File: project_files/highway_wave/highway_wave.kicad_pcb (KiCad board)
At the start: 2 copper layers, 138.2 x 87.8 mm, 36 parts, among them J1 Screw_Terminal_01x02, J10 Conn_01x02_Socket, J11 Conn_01x24, J12 Conn_01x24, J13 Screw_Terminal_01x02, J2 Screw_Terminal_01x02, J3 Conn_01x02_Socket, J4 Conn_01x02_Socket, J5 Conn_01x02_Pin, J6 Conn_01x02_Pin, J7 Conn_01x02_Pin, J8 Conn_01x04_Socket, J9 Conn_01x02_Pin, U1 TPS75633KC, U2 MOUDLE-BLUETOOTH-AUDIO-BC127_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, U4 PAM8403D

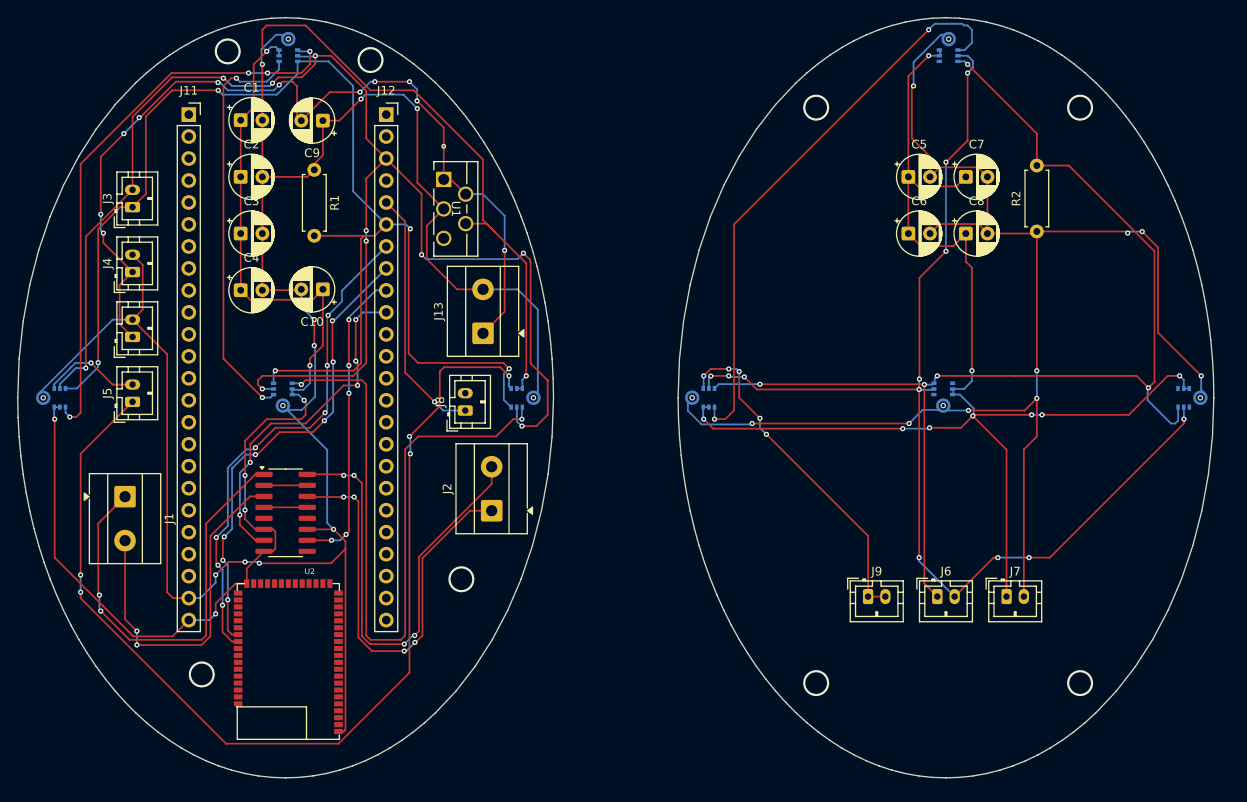
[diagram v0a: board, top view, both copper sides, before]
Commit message: moved caps on PCB
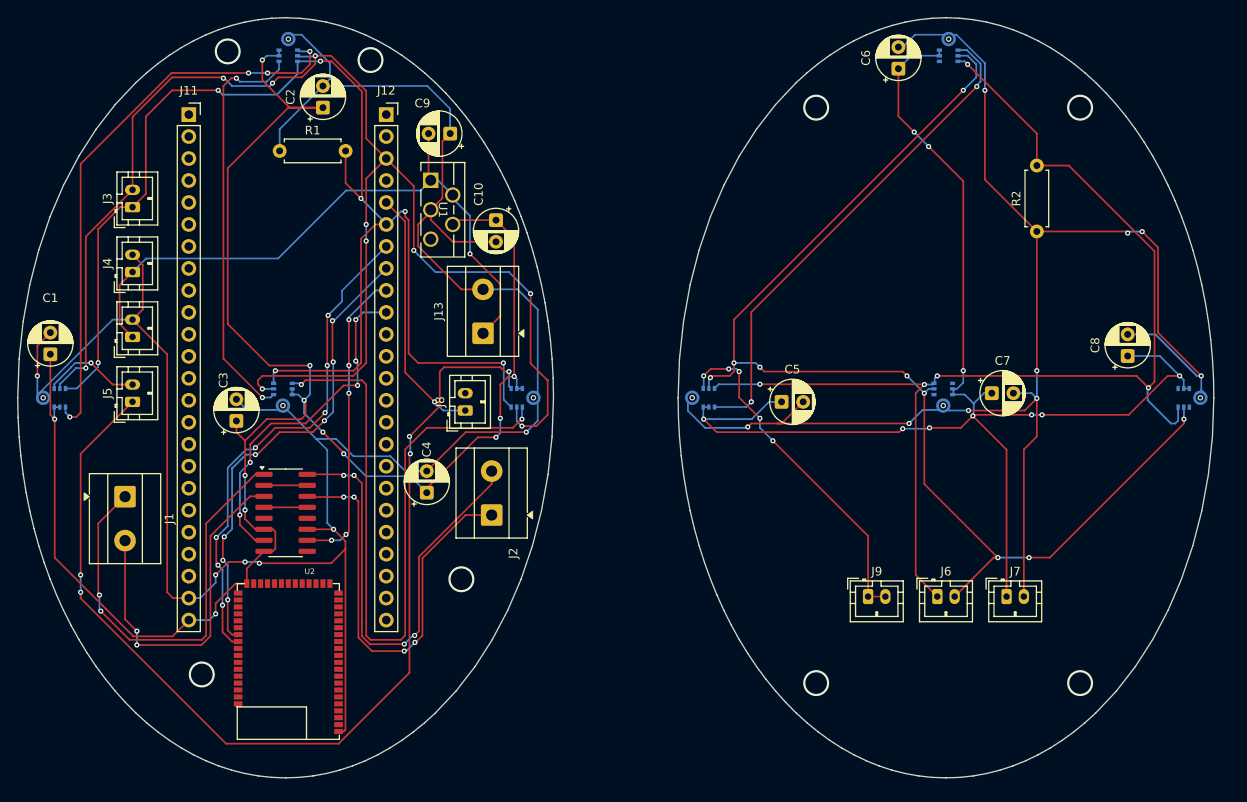
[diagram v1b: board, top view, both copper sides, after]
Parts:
- moved C1 34.9 mm to (74.0, 86.0), turned to 90 degrees
- moved C4 31.8 mm to (117.5, 102.0), turned to 90 degrees
- moved C5 29.8 mm to (158.5, 91.5)
- moved C7 25.2 mm to (182.8, 90.5)
- moved C8 23.5 mm to (198.5, 86.2), turned to 90 degrees
- moved C3 21.7 mm to (95.5, 93.7), turned to 90 degrees
- moved C10 21.5 mm to (125.5, 70.5), turned to -90 degrees
- moved C6 19.1 mm to (172.0, 53.0), turned to 90 degrees
- moved C9 14.8 mm to (120.2, 60.5)
- moved C2 12.4 mm to (105.5, 57.5), turned to 90 degrees
- moved R1 4.56 mm to (100.5, 62.5), turned to 0 degrees
- moved U1 1.50 mm to (118.0, 65.9)
- moved J2 0.50 mm to (125.0, 104.6)
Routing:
- net IN_3V3: track 105.8 -> 75.6 mm, vias 11 -> 1
- net Vout from Bat reg: track 204.5 -> 217.5 mm, vias 8 -> 12
- net IN_GND: track 245.9 -> 257.1 mm, vias 9 -> 6
- net WSO Mk5: track 66.3 -> 57.8 mm
- net Net-(J7-Pin_1): track 148.4 -> 156.5 mm, vias 9 -> 10
- net Net-(J6-Pin_2): track 133.0 -> 137.9 mm, vias 12 -> 9
- net Net-(J7-Pin_2): track 165.7 -> 169.8 mm
- net 36_IOB29B: track 170.7 -> 168.2 mm
- net 26_IOB8B: track 153.9 -> 156.1 mm, vias 5 -> 7
- net Net-(J6-Pin_1): track 134.5 -> 135.3 mm
- net Net-(J2-Pin_2): track 54.5 -> 54.0 mm
- net Net-(J2-Pin_1): track 49.9 -> 50.4 mm
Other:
- board text added: "(L)"
- board text added: "(R)"
- board text added: "w a v e"

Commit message: update BOM
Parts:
- removed C10: 47 uF, Capacitor_THT:CP_Radial_D5.0mm_P2.50mm
- removed C9: 1 uF, Capacitor_THT:CP_Radial_D5.0mm_P2.50mm
- removed the J1 at (82.6, 102.5)
- removed the J10 at (83.5, 84.0)
- removed the J2 at (125.0, 104.6)
- removed the J4 at (83.5, 76.5)
- removed U1: TPS75633KC, footprints:KC5
- removed U2: MOUDLE-BLUETOOTH-AUDIO-BC127_51P-18X11.8MM_, MOUDLE-BLUETOOTH-AUDIO-BC127_51P-18X11.8MM_:LGA51-0.8-18X11.8MM
- removed U4: PAM8403D, Package_SO:SOP-16_3.9x9.9mm_P1.27mm
- added J11: Conn_01x02_Socket, Connector_JST:JST_PH_B2B-PH-K_1x02_P2.00mm_Vertical, F.Cu at (118.0, 84.0)
- added J12: Conn_01x02_Socket, Connector_JST:JST_PH_B2B-PH-K_1x02_P2.00mm_Vertical, F.Cu at (117.9, 90.6)
- added J14: Conn_01x02_Socket, Connector_JST:JST_PH_B2B-PH-K_1x02_P2.00mm_Vertical, F.Cu at (83.0, 111.5)
- added J15: Conn_01x02_Socket, Connector_JST:JST_PH_B2B-PH-K_1x02_P2.00mm_Vertical, F.Cu at (83.0, 118.0)
- added J16: Conn_01x02_Socket, Connector_JST:JST_PH_B2B-PH-K_1x02_P2.00mm_Vertical, F.Cu at (118.0, 97.5)
- added J17: Conn_01x02_Socket, Connector_JST:JST_PH_B2B-PH-K_1x02_P2.00mm_Vertical, F.Cu at (118.0, 104.0)
- added J18: Conn_01x02_Socket, Connector_JST:JST_PH_B2B-PH-K_1x02_P2.00mm_Vertical, F.Cu at (125.5, 95.5)
- added J19: Conn_01x02_Socket, Connector_JST:JST_PH_B2B-PH-K_1x02_P2.00mm_Vertical, F.Cu at (118.0, 62.4)
- added J20: Screw_Terminal_01x02, TerminalBlock_MetzConnect:TerminalBlock_MetzConnect_Type101_RT01602HBWC_1x02_P5.08mm_Horizontal, F.Cu at (98.9, 125.0)
- added J21: Screw_Terminal_01x02, TerminalBlock_MetzConnect:TerminalBlock_MetzConnect_Type101_RT01602HBWC_1x02_P5.08mm_Horizontal, F.Cu at (177.2, 124.8)
- added J22: Conn_01x02_Socket, Connector_JST:JST_PH_B2B-PH-K_1x02_P2.00mm_Vertical, F.Cu at (118.0, 68.9)
- added J23: Conn_01x02_Socket, Connector_JST:JST_PH_B2B-PH-K_1x02_P2.00mm_Vertical, F.Cu at (118.0, 75.5)
- added J24: Conn_01x02_Socket, Connector_JST:JST_PH_B2B-PH-K_1x02_P2.00mm_Vertical, F.Cu at (194.2, 114.8)
- added J25: Conn_01x02_Socket, Connector_JST:JST_PH_B2B-PH-K_1x02_P2.00mm_Vertical, F.Cu at (125.5, 101.5)
- added J7: Conn_01x02_Socket, Connector_JST:JST_PH_B2B-PH-K_1x02_P2.00mm_Vertical, F.Cu at (82.5, 75.6)
- added J9: Conn_01x02_Socket, Connector_JST:JST_PH_B2B-PH-K_1x02_P2.00mm_Vertical, F.Cu at (82.5, 82.2)
- C1, C2, C3, C4, C5, C6, C7, C8: footprint Capacitor_THT:CP_Radial_D5.0mm_P2.50mm -> Capacitor_THT:C_Disc_D5.0mm_W2.5mm_P5.00mm; moved to B.Cu
- J5: value Conn_01x02_Pin -> Conn_01x02_Socket
- J8: value Conn_01x04_Socket -> Conn_01x02_Pin
- moved J13 48.4 mm to (78.6, 100.5), turned to -90 degrees
- moved J8 32.6 mm to (113.5, 124.0), turned to 180 degrees
- moved J5 22.5 mm to (82.5, 69.0), turned to 0 degrees
- moved R2 18.5 mm to (175.8, 57.9), turned to -90 degrees
- moved R1 16.9 mm to (95.5, 78.6), turned to 90 degrees
- moved C4 16.4 mm to (125.1, 87.5), turned to 0 degrees
- moved C3 10.3 mm to (104.5, 88.7), turned to -90 degrees
- moved C1 9.49 mm to (77.0, 95.0), turned to 180 degrees
- moved C2 8.27 mm to (97.9, 54.3)
- moved J3 6.58 mm to (82.5, 62.5), turned to 0 degrees
- moved C8 5.45 mm to (203.6, 88.2), turned to 0 degrees
- moved C5 4.96 mm to (155.2, 95.2), turned to 180 degrees
- moved C6 4.37 mm to (175.8, 55.2)
- moved MK5 2.45 mm to (151.4, 91.8)
- moved MK6 2.00 mm to (179.6, 51.5)
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- renumbered J12 to J1, J9 to J10, J11 to J2, J6 to J4, J7 to J6
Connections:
- C1 pad 1: Vout from Bat reg -> IN_3V3
- C2 pad 1: Vout from Bat reg -> IN_3V3
- C3 pad 1: Vout from Bat reg -> IN_3V3
- C4 pad 1: Vout from Bat reg -> IN_3V3
- J1 pad 1: 38_IOB31B -> 63_IOR5A
- J1 pad 10: 30_IOB13B -> 77_IOT37A
- J1 pad 11: 33_IOB23A -> 76_IOT37B
- J1 pad 12: 34_IOB23B -> 75_IOT38A
- J1 pad 13: 40_IOB33B -> 74_IOT38B
- J1 pad 14: 35_IOB29A -> 73_IOT39A
- J1 pad 15: 41_IOB41A -> 72_IOT39B
- J1 pad 16: 42_IOB41B -> 71_IOT41A
- J1 pad 17: 51_IOR17B -> 70_IOT41B
- J1 pad 18: 53_IOR15B -> IN_5V
- J1 pad 19: 54_IOR15A -> 48_IOR24B
- J1 pad 2: 37_IOB31A -> 86_IOT8A
- J1 pad 20: 55_IOR14B -> 49_IOR24B
- J1 pad 21: 56_IOR14A -> 31_IOB15A
- J1 pad 22: 57_IOR13A -> 32_IOB15B
- J1 pad 23: 68_IOT42B -> IN_GND
- J1 pad 24: 69_IOT42A -> IN_3V3
- J1 pad 3: 36_IOB29B -> 85_IOT8B
- J1 pad 4: 39_IOB33A -> 84_IOT10A
- J1 pad 5: 25_IOB8A -> 83_IOT10B
- J1 pad 6: 26_IOB8B -> 82_IOT11A
- J1 pad 7: 27_IOB11A -> 81_IOT11B
- J1 pad 8: 28_IOB11B -> 80_IOT12A
- J1 pad 9: 29_IOB13A -> 79_IOT12B
- J2 pad 1: 63_IOR5A -> 38_IOB31B
- J2 pad 10: 77_IOT37A -> 30_IOB13B
- J2 pad 11: 76_IOT37B -> 33_IOB23A
- J2 pad 12: 75_IOT38A -> 34_IOB23B
- J2 pad 13: 74_IOT38B -> 40_IOB33B
- J2 pad 14: 73_IOT39A -> 35_IOB29A
- J2 pad 15: 72_IOT39B -> 41_IOB41A
- J2 pad 16: 71_IOT41A -> 42_IOB41B
- J2 pad 17: 70_IOT41B -> 51_IOR17B
- J2 pad 18: IN_5V -> 53_IOR15B
- J2 pad 19: 48_IOR24B -> 54_IOR15A
- J2 pad 2: 86_IOT8A -> 37_IOB31A
- J2 pad 20: 49_IOR24B -> 55_IOR14B
- J2 pad 21: 31_IOB15A -> 56_IOR14A
- J2 pad 22: 32_IOB15B -> 57_IOR13A
- J2 pad 23: IN_GND -> 68_IOT42B
- J2 pad 24: Vout from Bat reg -> 69_IOT42A
- J2 pad 3: 85_IOT8B -> 36_IOB29B
- J2 pad 4: 84_IOT10A -> 39_IOB33A
- J2 pad 5: 83_IOT10B -> 25_IOB8A
- J2 pad 6: 82_IOT11A -> 26_IOB8B
- J2 pad 7: 81_IOT11B -> 27_IOB11A
- J2 pad 8: 80_IOT12A -> 28_IOB11B
- J2 pad 9: 79_IOT12B -> 29_IOB13A
- J5 pad 1: Net-(J5-Pin_1) -> IN_3V3
- J5 pad 2: Net-(J5-Pin_2) -> IN_GND
- J8 pad 1: 25_IOB8A -> Net-(J8-Pin_1)
- MK1 pad 2: Vout from Bat reg -> IN_3V3
- MK1 pad 3: Vout from Bat reg -> IN_3V3
- MK1 pad 5: Net-(J5-Pin_2) -> Net-(J8-Pin_2)
- MK2 pad 2: Vout from Bat reg -> IN_3V3
- MK2 pad 3: Vout from Bat reg -> IN_3V3
- MK3 pad 2: Vout from Bat reg -> IN_3V3
- MK3 pad 3: Vout from Bat reg -> IN_3V3
- MK4 pad 1: Net-(J5-Pin_1) -> Net-(J8-Pin_1)
- MK4 pad 2: Vout from Bat reg -> IN_3V3
- MK4 pad 3: Vout from Bat reg -> IN_3V3
- MK7 pad 1: unconnected-(MK7-WSO-Pad1) -> WSO Mk7
- MK7 pad 5: unconnected-(MK7-WS-Pad5) -> WSO Mk6
- MK8 pad 5: unconnected-(MK8-WS-Pad5) -> WSO Mk7
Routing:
- net Vout from Bat reg: track 217.5 -> 0.00 mm, vias 12 -> 0
- net Net-(J5-Pin_1): track 120.3 -> 0.00 mm, vias 5 -> 0
- net IN_3V3: track 75.6 -> 194.5 mm, vias 1 -> 0
- net Net-(J8-Pin_2): track 0.00 -> 73.1 mm, vias 0 -> 1
- net 27_IOB11A: track 58.1 -> 0.00 mm, vias 7 -> 0
- net 28_IOB11B: track 54.6 -> 0.00 mm, vias 7 -> 0
- net Net-(J2-Pin_2): track 54.0 -> 0.00 mm, vias 4 -> 0
- net WSO Mk3: track 80.8 -> 29.3 mm
- net Net-(J2-Pin_1): track 50.4 -> 0.00 mm, vias 4 -> 0
- net Net-(J1-Pin_1): track 50.4 -> 0.00 mm, vias 2 -> 0
- net Net-(J1-Pin_2): track 41.2 -> 0.00 mm, vias 2 -> 0
- net Net-(J8-Pin_1): track 0.00 -> 40.2 mm, vias 0 -> 1
- net 36_IOB29B: track 168.2 -> 128.2 mm, vias 10 -> 4
- net 26_IOB8B: track 156.1 -> 116.8 mm, vias 7 -> 5
- net WSO Mk6: track 0.00 -> 39.0 mm, vias 0 -> 2
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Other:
- board size 138.2 x 87.8 mm -> 140 x 88.6 mm
